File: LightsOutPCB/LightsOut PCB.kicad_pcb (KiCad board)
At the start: 2 copper layers, 68.6 x 53.3 mm, 38 parts, among them J1 Power, J2 Digital/PWM, J3 Analog, J4 Digital/PWM, J5 Conn_01x04_Pin, SW1 B3W-4050, SW2 B3W-4050, U1 SN74HC595N

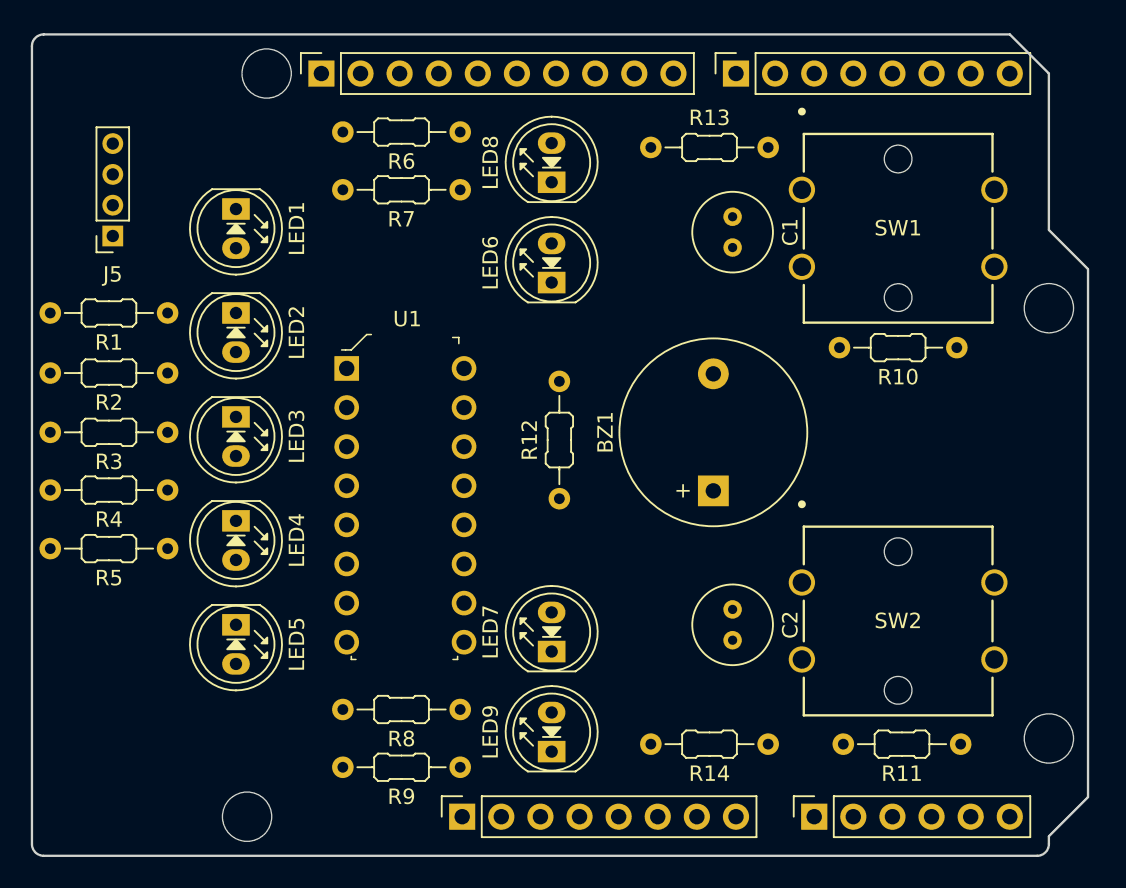
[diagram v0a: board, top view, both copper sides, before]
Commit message: set main traces
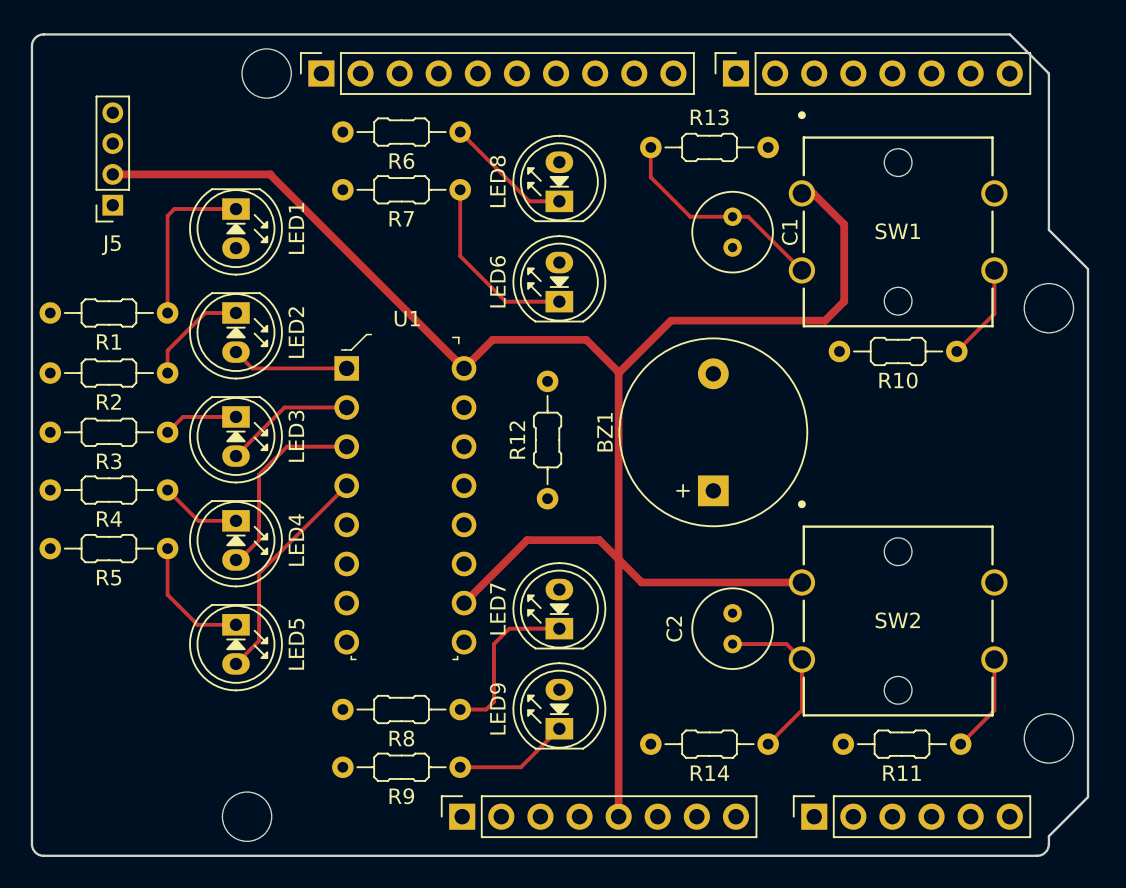
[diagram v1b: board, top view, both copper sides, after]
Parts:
- moved C2 2.25 mm to (145.5, 86.2), turned to 90 degrees
- moved J5 2.00 mm to (105.2, 57.8)
- moved LED7 1.57 mm to (134.2, 85.2)
- moved LED9 1.57 mm to (134.2, 91.8)
- moved LED6 1.34 mm to (134.2, 64.0)
- moved LED8 1.34 mm to (134.2, 57.5)
- moved R12 0.77 mm to (133.5, 76.8)
- moved R10 0.25 mm to (160.1, 67.2)
- moved SW1 0.23 mm to (150.0, 57.0)
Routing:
- net +5V: track 0.00 -> 118.5 mm
- net Net-(LED5-A): track 0.00 -> 14.5 mm
- net Net-(C1-Pad1): track 0.00 -> 14.3 mm
- net Net-(LED4-A): track 0.00 -> 12.7 mm
- net Net-(LED6-K): track 0.00 -> 12.0 mm
- net Net-(C2-Pad1): track 0.00 -> 11.3 mm
- net Net-(LED1-K): track 0.00 -> 10.9 mm
- net Net-(LED7-K): track 0.00 -> 10.8 mm
- net Net-(LED3-A): track 0.00 -> 8.49 mm
- net Net-(LED8-K): track 0.00 -> 8.30 mm
- net Net-(LED5-K): track 0.00 -> 8.25 mm
- net Net-(LED2-A): track 0.00 -> 7.63 mm
- net Net-(LED9-K): track 0.00 -> 7.48 mm
- net Net-(LED2-K): track 0.00 -> 6.91 mm
- net Net-(R11-Pad1): track 0.00 -> 6.41 mm
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
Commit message: routing complete
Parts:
- moved R12 19.0 mm to (152.5, 77.2), turned to 0 degrees
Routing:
- net /2: track 0.00 -> 70.2 mm
- net /5: track 0.00 -> 66.1 mm, vias 0 -> 1
- net /6: track 0.00 -> 59.6 mm, vias 0 -> 2
- net /7: track 0.00 -> 55.5 mm, vias 0 -> 2
- net /11: track 0.00 -> 52.9 mm
- net /4: track 0.00 -> 44.6 mm, vias 0 -> 1
- net /8: track 0.00 -> 36.7 mm, vias 0 -> 1
- net Net-(LED1-A): track 0.00 -> 19.1 mm
- net /SDA: track 0.00 -> 18.0 mm
- net /SCL: track 0.00 -> 15.2 mm
- net /9: track 0.00 -> 14.3 mm
- net /3: track 0.00 -> 10.1 mm
- net Net-(BZ1-+): track 0.00 -> 9.58 mm
- net /10: track 0.00 -> 7.04 mm
- net +5V: track 118.5 -> 117.9 mm
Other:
- board size 68.6 x 53.3 mm -> 69 x 53.5 mm

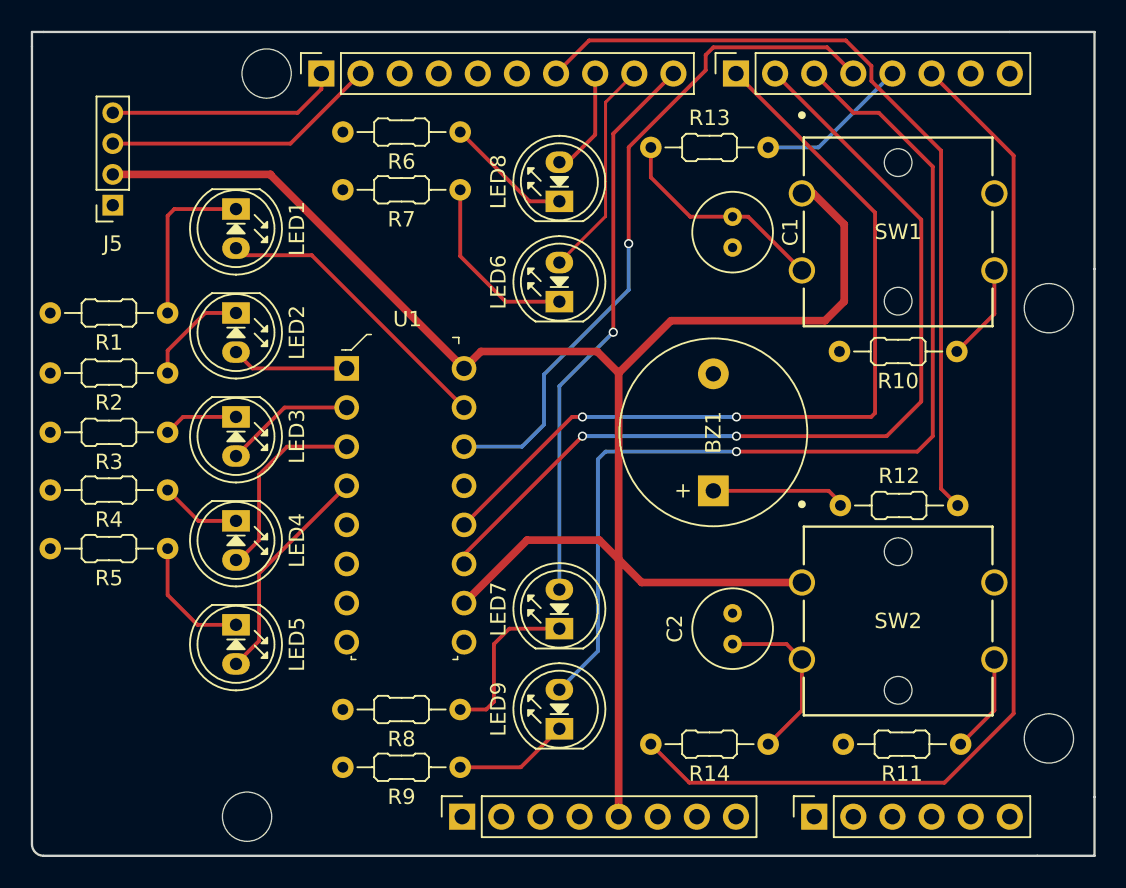
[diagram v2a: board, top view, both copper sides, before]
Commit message: Poured GND poly
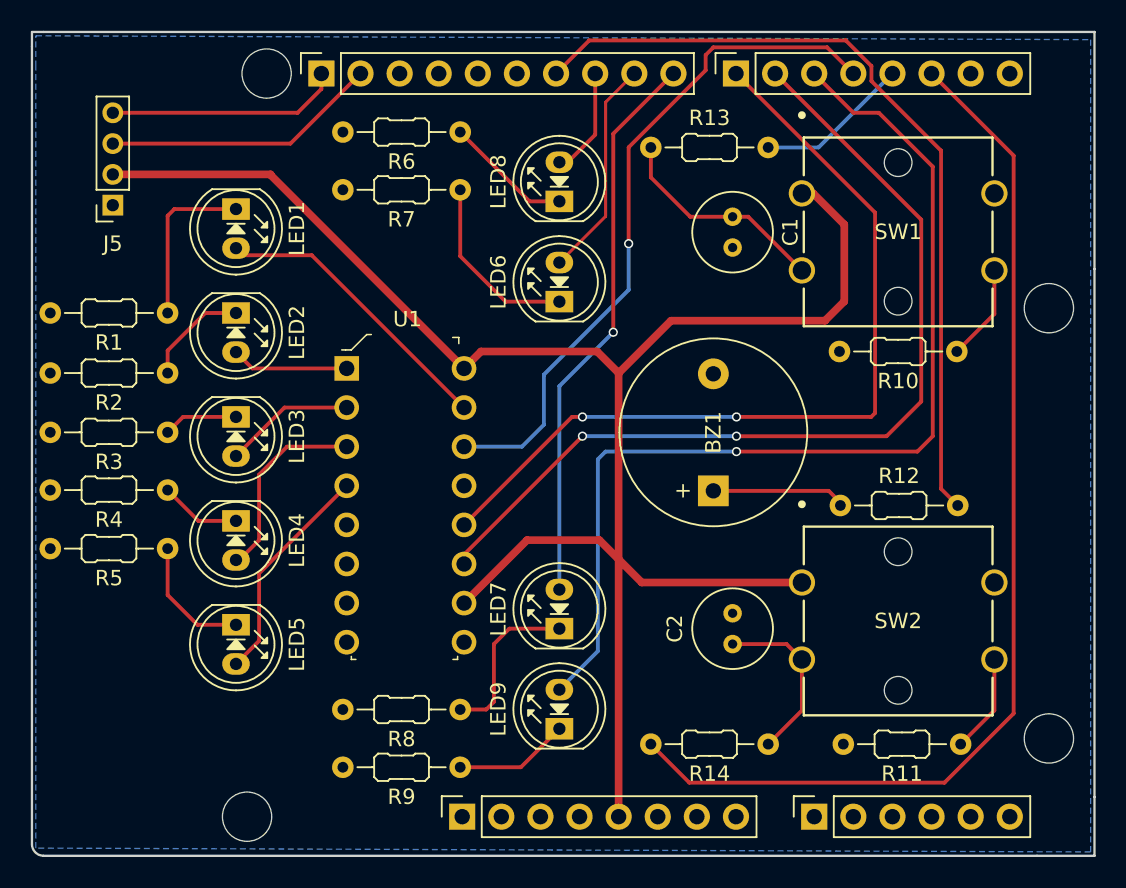
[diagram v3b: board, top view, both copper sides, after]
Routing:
- added copper zone on B.Cu, net GND
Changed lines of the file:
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@@
+	)
+	(segment
+		(start 158.42 49.2)
+		(end 163.75 54.53)
+		(width 0.25)
+		(layer "F.Cu")
+		(net "/2")
+	)
+	(segment
+		(start 159.259569 95.25)
+		(end 142.69 95.25)
+		(width 0.25)
+		(layer "F.Cu")
+		(net "/2")
+	)
+	(segment
+		(start 163.75 54.53)
+		(end 163.75 90.759569)
+		(width 0.25)
+		(layer "F.Cu")
+		(net "/2")
+	)
+	(segment
+		(start 163.75 90.759569)
+		(end 159.259569 95.25)
+		(width 0.25)
+		(layer "F.Cu")
+		(net "/2")
 	)
 	(segment
 		(start 142.69 95.25)
 		(end 140.19 92.75)
-		(width 0.25)
-		(layer "F.Cu")
-		(net "/2")
-	)
-	(segment
-		(start 163.75 54.53)
-		(end 163.75 90.759569)
-		(width 0.25)
-		(layer "F.Cu")
-		(net "/2")
-	)
-	(segment
-		(start 163.75 90.759569)
-		(end 159.259569 95.25)
-		(width 0.25)
-		(layer "F.Cu")
-		(net "/2")
-	)
-	(segment
-		(start 159.259569 95.25)
-		(end 142.69 95.25)
-		(width 0.25)
-		(layer "F.Cu")
-		(net "/2")
-	)
-	(segment
-		(start 158.42 49.2)
-		(end 163.75 54.53)
 		(width 0.25)
 		(layer "F.Cu")
@@
 		(net "Net-(R11-Pad1)")
 	)
+	(zone
+		(net "GND")
+		(layer "B.Cu")
+		(name "GND Pour")
+		(hatch edge 0.5)
+		(connect_pads
+			(clearance 0.508)
+		)
+		(min_thickness 0.25)
+		(fill yes
+			(thermal_gap 0.5)
+			(thermal_bridge_width 0.5)
+			(island_removal_mode 0)
+		)
+		(polygon
+			(pts
+				(xy 100.25 46.75) (xy 168.75 47) (xy 168.75 99.75) (xy 100.25 99.5) (xy 100.25 48.75)
+			)
+		)
+	)
 	(group ""

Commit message: info on front silkscreen
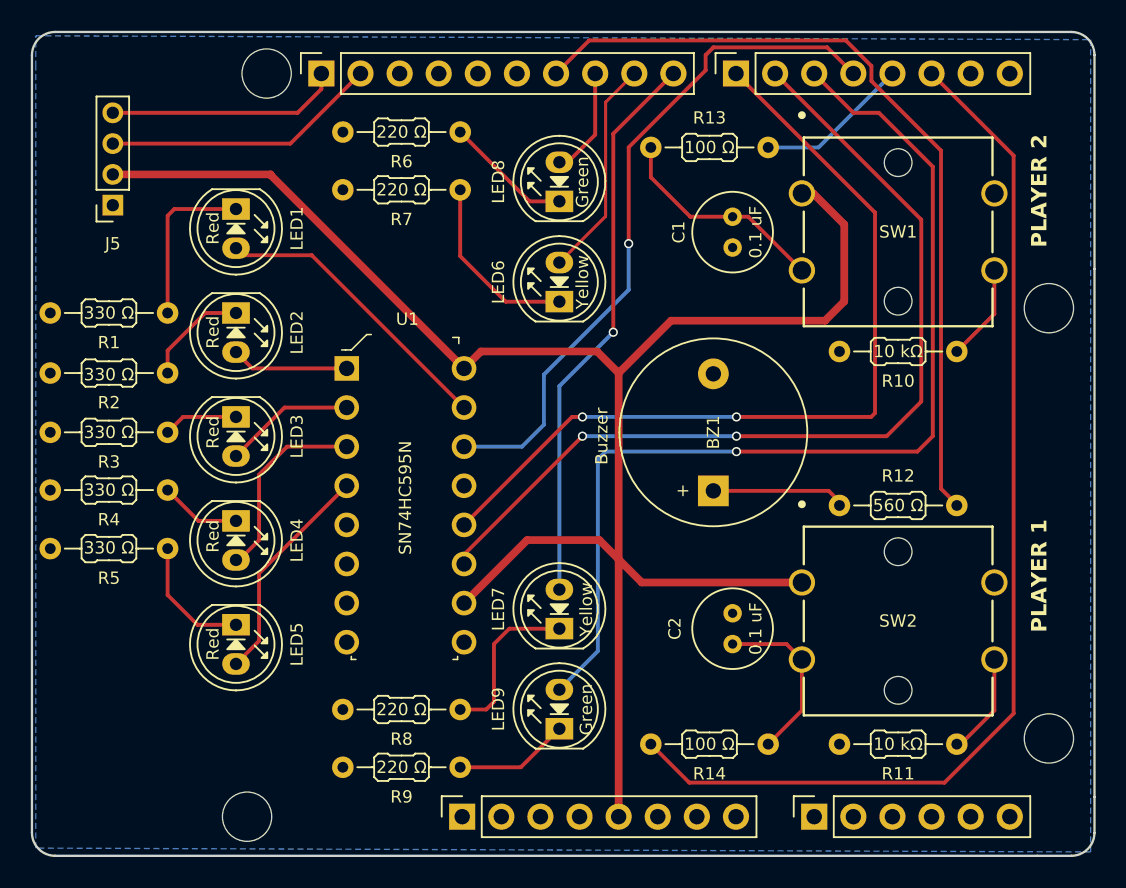
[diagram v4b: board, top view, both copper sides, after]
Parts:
- moved R11 0.25 mm to (160.1, 92.8)
- moved R12 0.06 mm to (152.4, 77.2)
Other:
- outline, holes or cut-outs redrawn
- board text added: "PLAYER 1"
- board text added: "PLAYER 2"

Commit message: added info to silkscreen
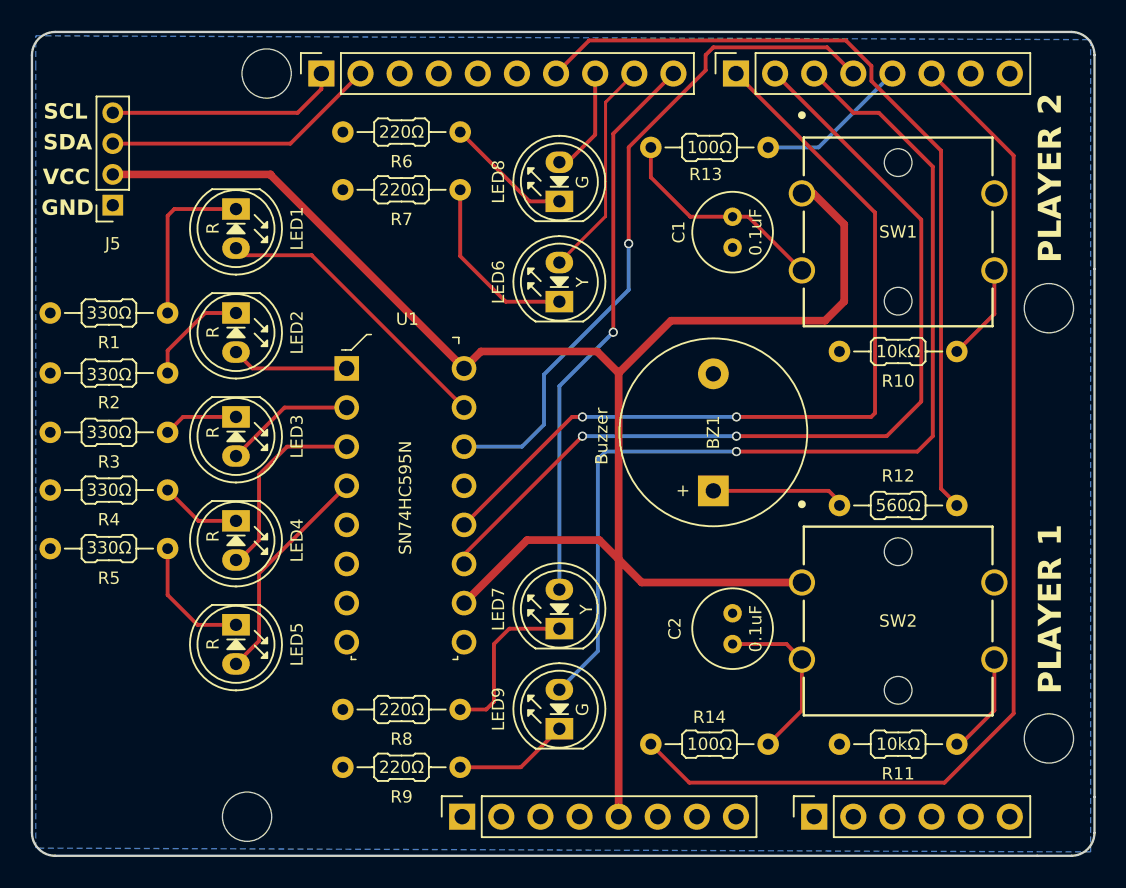
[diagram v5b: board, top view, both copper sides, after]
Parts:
- C1, C2: value 0.1 uF -> 0.1uF
- R1, R2, R3, R4, R5: value 330 Ω -> 330Ω
- R10, R11: value 10 kΩ -> 10kΩ
- R12: value 560 Ω -> 560Ω
- R13, R14: value 100 Ω -> 100Ω
- R6, R7, R8, R9: value 220 Ω -> 220Ω
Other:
- board text added: "GND"
- board text added: "Lights Out!"
- board text added: "Rev. 0.1"
- board text added: "SCL"
- board text added: "SDA"
- board text added: "Simply lovely"
- board text added: "VCC"
- board text added: "by kv151"
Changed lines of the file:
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@@
 			)
 		)
-		(property "Value" "330 Ω"
+		(property "Value" "330Ω"
 			(at 3.81 0 0)
 			(layer "F.SilkS")
@@
 			)
 		)
-		(property "Value" "10 kΩ"
+		(property "Value" "10kΩ"
 			(at 3.81 0 0)
 			(layer "F.SilkS")
@@
 			)
 		)
-		(property "Colour" "Red"
+		(property "Colour" "R"
 			(at 1 1.5 90)
 			(unlocked yes)
@@
 			)
 		)
-		(property "Value" "10 kΩ"
+		(property "Value" "10kΩ"
 			(at 3.81 0 0)
 			(layer "F.SilkS")
@@
 			)
 		)
-		(property "Value" "220 Ω"
+		(property "Value" "220Ω"
 			(at 3.81 0 0)
 			(layer "F.SilkS")
@@
 			)
 		)
-		(property "Colour" "Red"
+		(property "Colour" "R"
 			(at 1.25 1.5 90)
 			(unlocked yes)
@@
 			)
 		)
-		(property "Value" "220 Ω"
+		(property "Value" "220Ω"
 			(at 3.81 0 0)
 			(layer "F.SilkS")
@@
 			)
 		)
-		(property "Value" "220 Ω"
+		(property "Value" "220Ω"
 			(at 3.81 0 0)
 			(layer "F.SilkS")
@@
 			)
 		)
-		(property "Value" "0.1 uF"
+		(property "Value" "0.1uF"
 			(at 1 1.5 90)
 			(layer "F.SilkS")
@@
 			)
 		)
-		(property "Functionality Text" "Green"
+		(property "Functionality Text" "G"
 			(at 1.25 1.5 90)
 			(unlocked yes)
@@
 		(tags "Resistor Axial_DIN0204 series Axial Horizontal pin pitch 7.62mm 0.167W length 3.6mm diameter 1.6mm")
 		(property "Reference" "R14"
-			(at 3.81 -1.92 0)
+			(at 3.81 1.75 0)
 			(layer "F.SilkS")
 			(effects
@@
 			)
 		)
-		(property "Value" "100 Ω"
+		(property "Value" "100Ω"
 			(at 3.81 0 0)
 			(layer "F.SilkS")
@@
 			)
 		)
-		(property "Colour" "Red"
+		(property "Colour" "R"
 			(at 1.25 1.5 90)
 			(unlocked yes)
@@
 			)
 		)
-		(property "Value" "330 Ω"
+		(property "Value" "330Ω"
 			(at 3.81 0.05 0)
 			(layer "F.SilkS")
@@
 			)
 		)
-		(property "Value" "330 Ω"
+		(property "Value" "330Ω"
 			(at 3.81 0 0)
 			(layer "F.SilkS")
@@
 			)
 		)
-		(property "Value" "330 Ω"
+		(property "Value" "330Ω"
 			(at 3.81 -0.1 0)
 			(layer "F.SilkS")
@@
 			)
 		)
-		(property "Value" "220 Ω"
+		(property "Value" "220Ω"
 			(at 3.81 0 0)
 			(layer "F.SilkS")
@@
 			)
 		)
-		(property "Value" "330 Ω"
+		(property "Value" "330Ω"
 			(at 3.81 0 0)
 			(layer "F.SilkS")
@@
 			)
 		)
-		(property "Colour" "Green"
-			(at 1.25 1.75 90)
+		(property "Colour" "G"
+			(at 1.25 1.5 90)
 			(unlocked yes)
 			(layer "F.SilkS")
@@
 		(tags "Resistor Axial_DIN0204 series Axial Horizontal pin pitch 7.62mm 0.167W length 3.6mm diameter 1.6mm")
 		(property "Reference" "R13"
-			(at 3.81 -1.92 0)
+			(at 3.56 1.75 0)
 			(layer "F.SilkS")
 			(effects
@@
 			)
 		)
-		(property "Value" "100 Ω"
+		(property "Value" "100Ω"
 			(at 3.81 0 0)
 			(layer "F.SilkS")
@@
 			)
 		)
-		(property "Value" "0.1 uF"
+		(property "Value" "0.1uF"
 			(at 1 -1.5 90)
 			(layer "F.SilkS")
@@
 			)
 		)
-		(property "Colour" "Yellow"
+		(property "Colour" "Y"
 			(at 1.265 1.5 90)
 			(unlocked yes)
@@
 			)
 		)
-		(property "Value" "560 Ω"
+		(property "Value" "560Ω"
 			(at 3.81 0 0)
 			(layer "F.SilkS")
@@
 			)
 		)
-		(property "Colour" "Yellow"
+		(property "Colour" "Y"
 			(at 1.25 1.75 90)
 			(unlocked yes)
@@
 			)
 		)
-		(property "Field4" "Red"
+		(property "Field4" "R"
 			(at 1.25 1.5 90)
 			(unlocked yes)
@@
 			)
 		)
-		(property "Colour" "Red"
+		(property "Colour" "R"
 			(at 1 1.5 90)
 			(unlocked yes)
@@
 		(layer "Edge.Cuts")
 	)
-	(gr_text "PLAYER 2"
-		(at 166 60.5 90)
+	(gr_text "GND"
+		(at 100.607143 58.5 0)
 		(layer "F.SilkS")
 		(effects
 			(font
 				(size 1 1)
-				(thickness 0.2)
+				(thickness 0.25)
 				(bold yes)
 			)
@@
 		)
 	)
-	(gr_text "PLAYER 1"
-		(at 166 85.5 90)
+	(gr_text "VCC"
+		(at 100.702381 56.5 0)
 		(layer "F.SilkS")
 		(effects
 			(font
 				(size 1 1)
-				(thickness 0.2)
+				(thickness 0.25)
+				(bold yes)
+			)
+			(justify left bottom)
+		)
+	)
+	(gr_text "SDA"
+		(at 100.72619 54.25 0)
+		(layer "F.SilkS")
+		(effects
+			(font
+				(size 1 1)
+				(thickness 0.25)
+				(bold yes)
+			)
+			(justify left bottom)
+		)
+	)
+	(gr_text "SCL"
+		(at 100.75 52.25 0)
+		(layer "F.SilkS")
+		(effects
+			(font
+				(size 1 1)
+				(thickness 0.25)
+				(bold yes)
+			)
+			(justify left bottom)
+		)
+	)
+	(gr_text "PLAYER 2"
+		(at 167 61.5 90)
+		(layer "F.SilkS")
+		(effects
+			(font
+				(size 1.5 1.5)
+				(thickness 0.3)
 				(bold yes)
 			)
@@
 		)
 	)
+	(gr_text "PLAYER 1"
+		(at 167 89.5 90)
+		(layer "F.SilkS")
+		(effects
+			(font
+				(size 1.5 1.5)
+				(thickness 0.3)
+				(bold yes)
+			)
+			(justify left bottom)
+		)
+	)
+	(gr_text "Lights Out!"
+		(at 102.5 83.75 90)
+		(layer "B.SilkS")
+		(effects
+			(font
+				(size 1 1)
+				(thickness 0.15)
+			)
+			(justify left bottom mirror)
+		)
+	)
+	(gr_text "Rev. 0.1\n"
+		(at 104 83.75 90)
+		(layer "B.SilkS")
+		(effects
+			(font
+				(size 1 1)
+				(thickness 0.15)
+			)
+			(justify left bottom mirror)
+		)
+	)
+	(gr_text "by kv151"
+		(at 105.5 83.75 90)
+		(layer "B.SilkS")
+		(effects
+			(font
+				(size 1 1)
+				(thickness 0.15)
+			)
+			(justify left bottom mirror)
+		)
+	)
+	(gr_text "Simply lovely"
+		(at 124.5 72 90)
+		(layer "B.SilkS")
+		(effects
+			(font
+				(size 1 1)
+				(thickness 0.15)
+				(italic yes)
+			)
+			(justify left bottom mirror)
+		)
+	)

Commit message: Finsihed PCB design
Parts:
- added G***: LOGO, LightsOut Logo:smolLogo, F.Cu at (105.1, 92.5)
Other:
- board text added: "10"
- board text added: "11"
- board text added: "2"
- board text added: "4"
- board text added: "5V"
- board text added: "7"
- board text added: "8"
- board text added: "9"
- board text added: "~3"
- board text added: "~5"
- board text added: "~6"
- board text removed: "Lights Out!"
- board text removed: "Rev. 0.1"
